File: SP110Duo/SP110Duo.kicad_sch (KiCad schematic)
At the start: 247 parts, among them SW1 RotaryEncoder_Switch, SW10 Switch w/LED, SW100 Switch w/LED, SW101 Switch w/LED, SW102 Switch w/LED, SW103 Switch w/LED, SW104 Switch w/LED, SW105 Switch w/LED, SW106 Switch w/LED, SW107 Switch w/LED, SW108 Switch w/LED, SW109 Switch w/LED, SW11 Switch w/LED, SW110 Switch w/LED, SW12 Switch w/LED, SW13 Switch w/LED, SW14 Switch w/LED, SW15 Switch w/LED, SW16 Switch w/LED, SW17 Switch w/LED, SW18 Switch w/LED, SW19 Switch w/LED, SW2 Switch w/LED, SW20 Switch w/LED, SW21 Switch w/LED, SW22 Switch w/LED, SW23 Switch w/LED, SW24 Switch w/LED, SW25 Switch w/LED, SW26 Switch w/LED, SW27 Switch w/LED, SW28 Switch w/LED, SW29 Switch w/LED, SW3 Switch w/LED, SW30 Switch w/LED, SW31 Switch w/LED, SW32 Switch w/LED, SW33 Switch w/LED, SW34 Switch w/LED, SW35 Switch w/LED, SW36 Switch w/LED, SW37 Switch w/LED, SW38 Switch w/LED, SW39 Switch w/LED, SW4 Switch w/LED, SW40 Switch w/LED, SW41 Switch w/LED, SW42 Switch w/LED, SW43 Switch w/LED, SW44 Switch w/LED, SW45 Switch w/LED, SW46 Switch w/LED, SW47 Switch w/LED, SW48 Switch w/LED, SW49 Switch w/LED, SW5 Switch w/LED, SW50 Switch w/LED, SW51 Switch w/LED, SW52 Switch w/LED, SW53 Switch w/LED, SW54 Switch w/LED, SW55 Switch w/LED, SW56 Switch w/LED, SW57 Switch w/LED, SW58 Switch w/LED, SW59 Switch w/LED, SW6 Switch w/LED, SW60 Switch w/LED, SW61 RotaryEncoder_Switch, SW62 Switch w/LED, SW63 Switch w/LED, SW64 Switch w/LED, SW65 Switch w/LED, SW66 Switch w/LED, SW67 Switch w/LED, SW68 Switch w/LED, SW69 Switch w/LED, SW7 Switch w/LED, SW70 Switch w/LED, SW71 Switch w/LED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

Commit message: Update
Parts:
- SW1: renamed from SW2; footprint Greenwood:Hotswap_MX_Plated_LED_1u -> KeebLib:Hotswap_MX_Plated_LED_1u
- SW10: renamed from SW11; footprint Greenwood:Hotswap_MX_Plated_LED_1u -> KeebLib:Hotswap_MX_Plated_LED_1u
- SW100: footprint Greenwood:Hotswap_MX_Plated_LED_1.25u -> KeebLib:Hotswap_MX_Plated_LED_1.25u
- SW101, SW80: footprint Greenwood:Hotswap_MX_Plated_LED_2.25u -> KeebLib:Hotswap_MX_Plated_LED_2.25u
- SW102, SW103, SW104, SW105, SW106, SW107, SW108, SW109, SW110, SW20, SW21, SW22, SW23, SW24, SW25, SW26, SW27, SW28, SW29, SW30, SW31, SW32, SW33, SW34, SW35, SW36, SW37, SW38, SW40, SW41, SW42, SW44, SW45, SW46, SW47, SW48, SW49, SW50, SW51, SW52, SW53, SW54, SW55, SW57, SW58, SW59, SW60, SW77, SW78, SW79, SW81, SW82, SW83, SW84, SW85, SW86, SW87, SW88, SW89, SW90, SW92, SW93, SW94, SW95, SW96: footprint Greenwood:Hotswap_MX_Plated_LED_1u -> KeebLib:Hotswap_MX_Plated_LED_1u
- SW11: renamed from SW12; footprint Greenwood:Hotswap_MX_Plated_LED_1u -> KeebLib:Hotswap_MX_Plated_LED_1u
- SW12: renamed from SW13; footprint Greenwood:Hotswap_MX_Plated_LED_1u -> KeebLib:Hotswap_MX_Plated_LED_1u
- SW13: renamed from SW14; footprint Greenwood:Hotswap_MX_Plated_LED_1u -> KeebLib:Hotswap_MX_Plated_LED_1u
- SW14: renamed from SW15; footprint Greenwood:Hotswap_MX_Plated_LED_1u -> KeebLib:Hotswap_MX_Plated_LED_1u
- SW15: renamed from SW16; footprint Greenwood:Hotswap_MX_Plated_LED_1u -> KeebLib:Hotswap_MX_Plated_LED_1u
- SW16: renamed from SW17; footprint Greenwood:Hotswap_MX_Plated_LED_1u -> KeebLib:Hotswap_MX_Plated_LED_1u
- SW17: renamed from SW18; footprint Greenwood:Hotswap_MX_Plated_LED_1u -> KeebLib:Hotswap_MX_Plated_LED_1u
- SW18: renamed from SW19; footprint Greenwood:Hotswap_MX_Plated_LED_1u -> KeebLib:Hotswap_MX_Plated_LED_1u
- SW19: renamed from SW1; footprint Greenwood:RotaryEncoder_Alps_EC11E-Switch_Vertical_H20mm_Centred -> KeebLib:RotaryEncoder_Alps_EC11E-Switch_Vertical_H20mm_Centred
- SW2: renamed from SW3; footprint Greenwood:Hotswap_MX_Plated_LED_1u -> KeebLib:Hotswap_MX_Plated_LED_1u
- SW3: renamed from SW4; footprint Greenwood:Hotswap_MX_Plated_LED_1u -> KeebLib:Hotswap_MX_Plated_LED_1u
- SW39, SW76: footprint Greenwood:Hotswap_MX_Plated_LED_2u_90deg -> KeebLib:Hotswap_MX_Plated_LED_2u_90deg
- SW4: renamed from SW5; footprint Greenwood:Hotswap_MX_Plated_LED_1u -> KeebLib:Hotswap_MX_Plated_LED_1u
- SW43, SW56, SW97, SW98: footprint Greenwood:Hotswap_MX_Plated_LED_1.5u -> KeebLib:Hotswap_MX_Plated_LED_1.5u
- SW5: renamed from SW6; footprint Greenwood:Hotswap_MX_Plated_LED_1u -> KeebLib:Hotswap_MX_Plated_LED_1u
- SW6: renamed from SW7; footprint Greenwood:Hotswap_MX_Plated_LED_1u -> KeebLib:Hotswap_MX_Plated_LED_1u
- SW61: renamed from SW62; footprint Greenwood:Hotswap_MX_Plated_LED_1.75u -> KeebLib:Hotswap_MX_Plated_LED_1.75u
- SW62: renamed from SW63; footprint Greenwood:Hotswap_MX_Plated_LED_1u -> KeebLib:Hotswap_MX_Plated_LED_1u
- SW63: renamed from SW64; footprint Greenwood:Hotswap_MX_Plated_LED_1u -> KeebLib:Hotswap_MX_Plated_LED_1u
- SW64: renamed from SW65; footprint Greenwood:Hotswap_MX_Plated_LED_1u -> KeebLib:Hotswap_MX_Plated_LED_1u
- SW65: renamed from SW66; footprint Greenwood:Hotswap_MX_Plated_LED_1u -> KeebLib:Hotswap_MX_Plated_LED_1u
- SW66: renamed from SW67; footprint Greenwood:Hotswap_MX_Plated_LED_1u -> KeebLib:Hotswap_MX_Plated_LED_1u
- SW67: renamed from SW68; footprint Greenwood:Hotswap_MX_Plated_LED_1u -> KeebLib:Hotswap_MX_Plated_LED_1u
- SW68: renamed from SW69; footprint Greenwood:Hotswap_MX_Plated_LED_1u -> KeebLib:Hotswap_MX_Plated_LED_1u
- SW69: renamed from SW70; footprint Greenwood:Hotswap_MX_Plated_LED_1u -> KeebLib:Hotswap_MX_Plated_LED_1u
- SW7: renamed from SW8; footprint Greenwood:Hotswap_MX_Plated_LED_1u -> KeebLib:Hotswap_MX_Plated_LED_1u
- SW70: renamed from SW71; footprint Greenwood:Hotswap_MX_Plated_LED_1u -> KeebLib:Hotswap_MX_Plated_LED_1u
- SW71: renamed from SW72; footprint Greenwood:Hotswap_MX_Plated_LED_1u -> KeebLib:Hotswap_MX_Plated_LED_1u
- SW72: renamed from SW73; footprint Greenwood:Hotswap_MX_Plated_LED_1u -> KeebLib:Hotswap_MX_Plated_LED_1u
- SW73: renamed from SW74; footprint Greenwood:Hotswap_MX_Plated_LED_2.25u -> KeebLib:Hotswap_MX_Plated_LED_2.25u
- SW74: renamed from SW75; footprint Greenwood:Hotswap_MX_Plated_LED_1u -> KeebLib:Hotswap_MX_Plated_LED_1u
- SW8: renamed from SW9; footprint Greenwood:Hotswap_MX_Plated_LED_1u -> KeebLib:Hotswap_MX_Plated_LED_1u
- SW9: renamed from SW10; footprint Greenwood:Hotswap_MX_Plated_LED_1u -> KeebLib:Hotswap_MX_Plated_LED_1u
- SW91: footprint Greenwood:Hotswap_MX_Plated_LED_1.75u -> KeebLib:Hotswap_MX_Plated_LED_1.75u
- SW99: footprint Greenwood:Hotswap_MX_Plated_LED_2.75u -> KeebLib:Hotswap_MX_Plated_LED_2.75u
- renumbered C5 to C10, C6 to C5, C7 to C6, C8 to C7, C9 to C8, C10 to C9, D2 to D1, D11 to D10, D12 to D11, D13 to D12, D14 to D13, D15 to D14, D16 to D15, D17 to D16, D18 to D17, D19 to D18, D1 to D19, D3 to D2, D4 to D3, D5 to D4, D6 to D5, D7 to D6, D62 to D61, D63 to D62, D64 to D63, D65 to D64, D66 to D65, D67 to D66, D68 to D67, D69 to D68, D70 to D69, D8 to D7, D71 to D70, D72 to D71, D73 to D72, D74 to D73, D75 to D74, D61 to D75, D9 to D8, D10 to D9, RESET to RESET1, SW61 to SW75, U3 to U2, U2 to U3

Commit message: change name
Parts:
- removed C5: 100uF, Capacitor_Tantalum_SMD:CP_EIA-6032-15_Kemet-U_Pad2.25x2.35mm_HandSolder, symbol Device:C_Polarized
- added R4, R5, R6: 5.1k, Resistor_SMD:R_1206_3216Metric_Pad1.30x1.75mm_HandSolder, symbol Device:R
- SW61: renamed from SW75; footprint Greenwood:EVQWGD001 -> KeebLib:RotaryEncoder_Alps_EC11E-Switch_Vertical_H20mm_Centred
- U3: footprint ScottoKeebs_MCU:Raspberry_Pi_Pico -> KeebLib:Raspberry_Pi_Pico_Flipped_No_Pads
- renumbered C10 to C5, D19 to D1, D9 to D10, D10 to D11, D11 to D12, D12 to D13, D13 to D14, D14 to D15, D15 to D16, D16 to D17, D17 to D18, D18 to D19, D1 to D2, D2 to D3, D3 to D4, D4 to D5, D5 to D6, D75 to D61, D61 to D62, D62 to D63, D63 to D64, D64 to D65, D65 to D66, D66 to D67, D67 to D68, D68 to D69, D6 to D7, D69 to D70, D70 to D71, D71 to D72, D72 to D73, D73 to D74, D74 to D75, D7 to D8, D8 to D9, H2 to H1, H3 to H2, H4 to H3, H5 to H4, H1 to H5, SW19 to SW1, SW9 to SW10, SW10 to SW11, SW11 to SW12, SW12 to SW13, SW13 to SW14, SW14 to SW15, SW15 to SW16, SW16 to SW17, SW17 to SW18, SW18 to SW19, SW1 to SW2, SW2 to SW3, SW3 to SW4, SW4 to SW5, SW5 to SW6, SW61 to SW62, SW62 to SW63, SW63 to SW64, SW64 to SW65, SW65 to SW66, SW66 to SW67, SW67 to SW68, SW68 to SW69, SW6 to SW7, SW69 to SW70, SW70 to SW71, SW71 to SW72, SW72 to SW73, SW73 to SW74, SW74 to SW75, SW7 to SW8, SW8 to SW9
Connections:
- net ENC1_A: now also C3.2, R4.1; no longer C3.1, SW1.A
- net ENC2_A: now also C5.2, U3.21 (GPIO16), R6.1; no longer C4.1, SW61.A, U3.19 (GPIO14)
- net ENC_B: now also C4.1, R5.1; no longer C5.1, SW1.B, SW61.B
- net GND: now also C3.1, C5.1; no longer C3.2, C5.2
- net OLED_CS: now also U3.22 (GPIO17); no longer U3.21 (GPIO16)
- net OLED_DC: now also U3.24 (GPIO18); no longer U3.22 (GPIO17)
- net OLED_RESET: now also U3.19 (GPIO14); no longer U3.24 (GPIO18)
- new net ROT1_A: R4.2, SW1.A
- new net ROT2_A: R6.2, SW61.A
- new net ROT_B: R5.2, SW1.B, SW61.B
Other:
- note added: "Encoders"
- note removed: "Encoder Filters"
- moved on the sheet: C3, C4, C5, C6, C7, C8, C9, D1, D61, H1, H2, H3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

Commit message: Update diode directions
Correct diode direction so that columns are not reversed in software.
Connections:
- net ROW0: now also D1.2 (A), D10.2 (A), D11.1 (K), D12.2 (A), D13.1 (K), D14.2 (A), D15.1 (K), D16.2 (A), D17.1 (K), D18.2 (A), D19.1 (K), D2.1 (K), D3.2 (A), D4.1 (K), D5.1 (K), D6.2 (A), D7.1 (K), D8.2 (A), D9.1 (K); no longer D1.1 (K), D10.1 (K), D11.2 (A), D12.1 (K), D13.2 (A), D14.1 (K), D15.2 (A), D16.1 (K), D17.2 (A), D18.1 (K), D19.2 (A), D2.2 (A), D3.1 (K), D4.2 (A), D5.2 (A), D6.1 (K), D7.2 (A), D8.1 (K), D9.2 (A)
- net ROW1: now also D20.2 (A), D21.1 (K), D22.2 (A), D23.1 (K), D24.1 (K), D25.2 (A), D26.1 (K), D27.2 (A), D28.1 (K), D29.2 (A), D30.1 (K), D31.2 (A), D32.1 (K), D33.2 (A), D34.1 (K), D35.2 (A), D36.1 (K), D37.2 (A), D38.1 (K); no longer D20.1 (K), D21.2 (A), D22.1 (K), D23.2 (A), D24.2 (A), D25.1 (K), D26.2 (A), D27.1 (K), D28.2 (A), D29.1 (K), D30.2 (A), D31.1 (K), D32.2 (A), D33.1 (K), D34.2 (A), D35.1 (K), D36.2 (A), D37.1 (K), D38.2 (A)
- net ROW2: now also D39.2 (A), D40.1 (K), D41.2 (A), D42.1 (K), D43.1 (K), D44.2 (A), D45.1 (K), D46.2 (A), D47.1 (K), D48.2 (A), D49.1 (K), D50.2 (A), D51.1 (K), D52.2 (A), D53.1 (K), D54.2 (A), D55.1 (K), D56.2 (A), D57.1 (K); no longer D39.1 (K), D40.2 (A), D41.1 (K), D42.2 (A), D43.2 (A), D44.1 (K), D45.2 (A), D46.1 (K), D47.2 (A), D48.1 (K), D49.2 (A), D50.1 (K), D51.2 (A), D52.1 (K), D53.2 (A), D54.1 (K), D55.2 (A), D56.1 (K), D57.2 (A)
- net ROW3: now also D58.1 (K), D59.2 (A), D60.1 (K), D61.2 (A), D62.1 (K), D63.2 (A), D64.1 (K), D65.2 (A), D66.1 (K), D67.2 (A), D68.1 (K), D69.2 (A), D70.1 (K), D71.2 (A), D72.1 (K), D73.2 (A), D74.1 (K), D75.1 (K); no longer D58.2 (A), D59.1 (K), D60.2 (A), D61.1 (K), D62.2 (A), D63.1 (K), D64.2 (A), D65.1 (K), D66.2 (A), D67.1 (K), D68.2 (A), D69.1 (K), D70.2 (A), D71.1 (K), D72.2 (A), D73.1 (K), D74.2 (A), D75.2 (A)
- net ROW4: now also D76.2 (A), D77.1 (K), D78.2 (A), D79.1 (K), D80.1 (K), D81.1 (K), D82.2 (A), D83.1 (K), D84.2 (A), D85.1 (K), D86.2 (A), D87.1 (K), D88.2 (A), D89.1 (K), D90.2 (A), D91.1 (K), D92.1 (K), D93.2 (A), D94.2 (A); no longer D76.1 (K), D77.2 (A), D78.1 (K), D79.2 (A), D80.2 (A), D81.2 (A), D82.1 (K), D83.2 (A), D84.1 (K), D85.2 (A), D86.1 (K), D87.2 (A), D88.1 (K), D89.2 (A), D90.1 (K), D91.2 (A), D92.2 (A), D93.1 (K), D94.1 (K)
- net ROW5: now also D100.1 (K), D101.1 (K), D102.2 (A), D103.1 (K), D104.2 (A), D105.1 (K), D106.2 (A), D107.1 (K), D108.1 (K), D109.2 (A), D110.1 (K), D95.1 (K), D96.2 (A), D97.2 (A), D98.1 (K), D99.1 (K); no longer D100.2 (A), D101.2 (A), D102.1 (K), D103.2 (A), D104.1 (K), D105.2 (A), D106.1 (K), D107.2 (A), D108.2 (A), D109.1 (K), D110.2 (A), D95.2 (A), D96.1 (K), D97.1 (K), D98.2 (A), D99.2 (A)
- net at SW92.2: now also D92.2 (A); no longer D92.1 (K)
- net at SW32.2: now also D32.2 (A); no longer D32.1 (K)
- net at SW61.S1: now also D61.1 (K); no longer D61.2 (A)
- net at SW108.2: now also D108.2 (A); no longer D108.1 (K)
- net at SW13.2: now also D13.2 (A); no longer D13.1 (K)
- net at SW22.2: now also D22.1 (K); no longer D22.2 (A)
- net at SW80.2: now also D80.2 (A); no longer D80.1 (K)
- net at SW17.2: now also D17.2 (A); no longer D17.1 (K)
- net at SW101.2: now also D101.2 (A); no longer D101.1 (K)
- net at SW75.2: now also D75.2 (A); no longer D75.1 (K)
- net at SW46.2: now also D46.1 (K); no longer D46.2 (A)
- net at SW82.2: now also D82.1 (K); no longer D82.2 (A)
- net at SW67.2: now also D67.1 (K); no longer D67.2 (A)
- net at SW76.2: now also D76.1 (K); no longer D76.2 (A)
- net at SW40.2: now also D40.2 (A); no longer D40.1 (K)
- net at SW14.2: now also D14.1 (K); no longer D14.2 (A)
- net at SW2.2: now also D2.2 (A); no longer D2.1 (K)
- net at SW66.2: now also D66.2 (A); no longer D66.1 (K)
- net at SW41.2: now also D41.1 (K); no longer D41.2 (A)
- net at SW79.2: now also D79.2 (A); no longer D79.1 (K)
- net at SW93.2: now also D93.1 (K); no longer D93.2 (A)
- net at SW45.2: now also D45.2 (A); no longer D45.1 (K)
- net at SW11.2: now also D11.2 (A); no longer D11.1 (K)
- net at SW99.2: now also D99.2 (A); no longer D99.1 (K)
- net at SW71.2: now also D71.1 (K); no longer D71.2 (A)
- net at SW96.2: now also D96.1 (K); no longer D96.2 (A)
- net at SW65.2: now also D65.1 (K); no longer D65.2 (A)
- net at SW57.2: now also D57.2 (A); no longer D57.1 (K)
- net at SW25.2: now also D25.1 (K); no longer D25.2 (A)
- net at SW77.2: now also D77.2 (A); no longer D77.1 (K)
- net at SW4.2: now also D4.2 (A); no longer D4.1 (K)
- net at SW60.2: now also D60.2 (A); no longer D60.1 (K)
- net at SW36.2: now also D36.2 (A); no longer D36.1 (K)
- net at SW81.2: now also D81.2 (A); no longer D81.1 (K)
- net at SW70.2: now also D70.2 (A); no longer D70.1 (K)
- net at SW87.2: now also D87.2 (A); no longer D87.1 (K)
- net at SW95.2: now also D95.2 (A); no longer D95.1 (K)
- net at SW48.2: now also D48.1 (K); no longer D48.2 (A)
- net at SW83.2: now also D83.2 (A); no longer D83.1 (K)
- net at SW52.2: now also D52.1 (K); no longer D52.2 (A)
- net at SW68.2: now also D68.2 (A); no longer D68.1 (K)
- net at SW107.2: now also D107.2 (A); no longer D107.1 (K)
- net at SW56.2: now also D56.1 (K); no longer D56.2 (A)
- net at SW39.2: now also D39.1 (K); no longer D39.2 (A)
- net at SW21.2: now also D21.2 (A); no longer D21.1 (K)
- net at SW94.2: now also D94.1 (K); no longer D94.2 (A)
- net at SW74.2: now also D74.2 (A); no longer D74.1 (K)
- net at SW72.2: now also D72.2 (A); no longer D72.1 (K)
- net at SW44.2: now also D44.1 (K); no longer D44.2 (A)
- net at SW35.2: now also D35.1 (K); no longer D35.2 (A)
- net at SW6.2: now also D6.1 (K); no longer D6.2 (A)
- net at SW15.2: now also D15.2 (A); no longer D15.1 (K)
- net at SW3.2: now also D3.1 (K); no longer D3.2 (A)
- net at SW110.2: now also D110.2 (A); no longer D110.1 (K)
- net at SW33.2: now also D33.1 (K); no longer D33.2 (A)
- net at SW59.2: now also D59.1 (K); no longer D59.2 (A)
- net at SW55.2: now also D55.2 (A); no longer D55.1 (K)
- net at SW98.2: now also D98.2 (A); no longer D98.1 (K)
- net at SW88.2: now also D88.1 (K); no longer D88.2 (A)
- net at SW91.2: now also D91.2 (A); no longer D91.1 (K)
- net at SW78.2: now also D78.1 (K); no longer D78.2 (A)
- net at SW20.2: now also D20.1 (K); no longer D20.2 (A)
- net at SW42.2: now also D42.2 (A); no longer D42.1 (K)
- net at SW7.2: now also D7.2 (A); no longer D7.1 (K)
- net at SW105.2: now also D105.2 (A); no longer D105.1 (K)
- net at SW43.2: now also D43.2 (A); no longer D43.1 (K)
- net at SW53.2: now also D53.2 (A); no longer D53.1 (K)
- net at SW9.2: now also D9.2 (A); no longer D9.1 (K)
- net at SW37.2: now also D37.1 (K); no longer D37.2 (A)
- net at SW28.2: now also D28.2 (A); no longer D28.1 (K)
- net at SW62.2: now also D62.2 (A); no longer D62.1 (K)
- net at SW84.2: now also D84.1 (K); no longer D84.2 (A)
- net at SW8.2: now also D8.1 (K); no longer D8.2 (A)
- net at SW26.2: now also D26.2 (A); no longer D26.1 (K)
- net at SW18.2: now also D18.1 (K); no longer D18.2 (A)
- net at SW97.2: now also D97.1 (K); no longer D97.2 (A)
- net at SW23.2: now also D23.2 (A); no longer D23.1 (K)
- net at SW69.2: now also D69.1 (K); no longer D69.2 (A)
- net at SW19.2: now also D19.2 (A); no longer D19.1 (K)
- net at SW102.2: now also D102.1 (K); no longer D102.2 (A)
- net at SW49.2: now also D49.2 (A); no longer D49.1 (K)
- net at SW12.2: now also D12.1 (K); no longer D12.2 (A)
- net at SW85.2: now also D85.2 (A); no longer D85.1 (K)
- net at SW51.2: now also D51.2 (A); no longer D51.1 (K)
- net at SW103.2: now also D103.2 (A); no longer D103.1 (K)
- net at SW86.2: now also D86.1 (K); no longer D86.2 (A)
- net at SW38.2: now also D38.2 (A); no longer D38.1 (K)
- net at SW63.2: now also D63.1 (K); no longer D63.2 (A)
- net at SW30.2: now also D30.2 (A); no longer D30.1 (K)
- net at SW106.2: now also D106.1 (K); no longer D106.2 (A)
- net at SW50.2: now also D50.1 (K); no longer D50.2 (A)
- net at SW104.2: now also D104.1 (K); no longer D104.2 (A)
- net at SW90.2: now also D90.1 (K); no longer D90.2 (A)
- net at SW5.2: now also D5.2 (A); no longer D5.1 (K)
- net at SW109.2: now also D109.1 (K); no longer D109.2 (A)
- net at SW34.2: now also D34.2 (A); no longer D34.1 (K)
- net at SW100.2: now also D100.2 (A); no longer D100.1 (K)
- net at SW89.2: now also D89.2 (A); no longer D89.1 (K)
- net at SW16.2: now also D16.1 (K); no longer D16.2 (A)
- net at SW29.2: now also D29.1 (K); no longer D29.2 (A)
- net at SW1.S1: now also D1.1 (K); no longer D1.2 (A)
- net at SW64.2: now also D64.2 (A); no longer D64.1 (K)
- net at SW58.2: now also D58.2 (A); no longer D58.1 (K)
- net at SW24.2: now also D24.2 (A); no longer D24.1 (K)
- net at SW47.2: now also D47.2 (A); no longer D47.1 (K)
- net at SW27.2: now also D27.1 (K); no longer D27.2 (A)
- net at SW73.2: now also D73.1 (K); no longer D73.2 (A)
- net at SW31.2: now also D31.1 (K); no longer D31.2 (A)
- net at SW10.2: now also D10.1 (K); no longer D10.2 (A)
- net at SW54.2: now also D54.1 (K); no longer D54.2 (A)
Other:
- moved on the sheet: D1, D10, D100, D101, D102, D103, D104, D105, D106, D107, D108, D109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

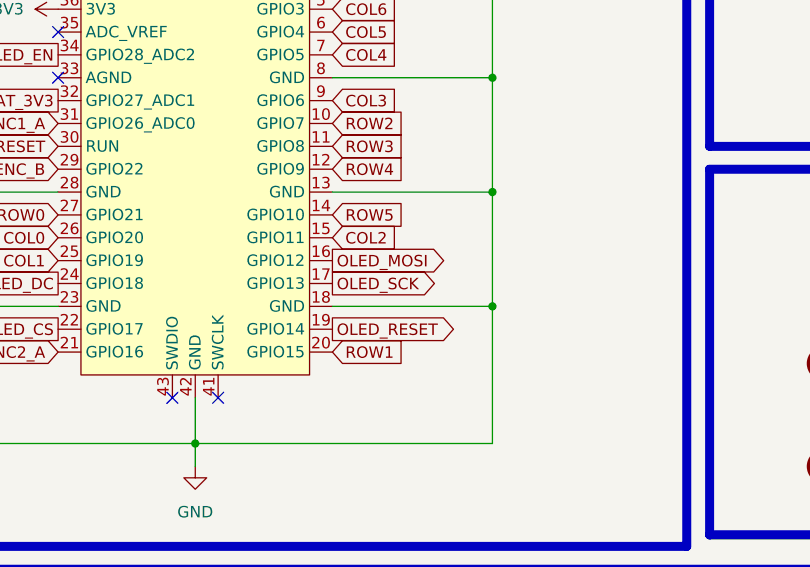
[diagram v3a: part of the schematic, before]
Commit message: Fix crossed pins for display
Update so that SPI pins are in correct place
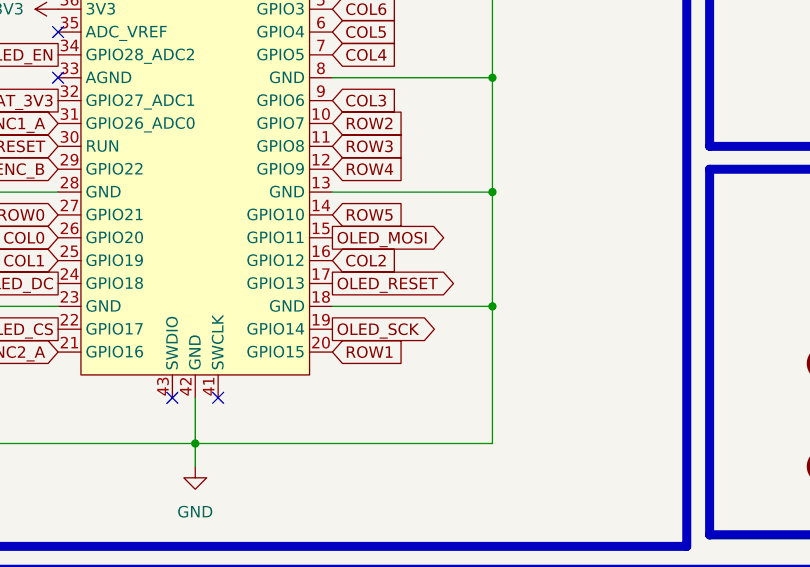
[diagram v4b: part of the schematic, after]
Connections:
- net COL2: now also U3.16 (GPIO12); no longer U3.15 (GPIO11)
- net OLED_MOSI: now also U3.15 (GPIO11); no longer U3.16 (GPIO12)
- net OLED_RESET: now also U3.17 (GPIO13); no longer U3.19 (GPIO14)
- net OLED_SCK: now also U3.19 (GPIO14); no longer U3.17 (GPIO13)
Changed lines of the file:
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@@
     )
   )
-  (global_label "COL2" (shape input) (at 175.26 151.13 0) (fields_autoplaced)
-    (effects (font (size 1.27 1.27)) (justify left))
-    (property "Intersheetrefs" "${INTERSHEET_REFS}" (at 183.0833 151.13 0)
+  (global_label "COL2" (shape input) (at 175.26 153.67 0) (fields_autoplaced)
+    (effects (font (size 1.27 1.27)) (justify left))
+    (property "Intersheetrefs" "${INTERSHEET_REFS}" (at 183.0833 153.67 0)
       (effects (font (size 1.27 1.27)) (justify left) hide)
     )
@@
     )
   )
-  (global_label "OLED_SCK" (shape output) (at 175.26 156.21 0) (fields_autoplaced)
-    (effects (font (size 1.27 1.27)) (justify left))
-    (property "Intersheetrefs" "${INTERSHEET_REFS}" (at 187.7399 156.21 0)
-      (effects (font (size 1.27 1.27)) (justify left) hide)
-    )
-  )
   (global_label "COL1" (shape input) (at 144.78 153.67 180) (fields_autoplaced)
     (effects (font (size 1.27 1.27)) (justify right))
@@
     )
   )
+  (global_label "OLED_SCK" (shape output) (at 175.26 161.29 0) (fields_autoplaced)
+    (effects (font (size 1.27 1.27)) (justify left))
+    (property "Intersheetrefs" "${INTERSHEET_REFS}" (at 187.7399 161.29 0)
+      (effects (font (size 1.27 1.27)) (justify left) hide)
+    )
+  )
   (global_label "COL3" (shape input) (at 175.26 135.89 0) (fields_autoplaced)
     (effects (font (size 1.27 1.27)) (justify left))
@@
     )
   )
-  (global_label "OLED_MOSI" (shape output) (at 175.26 153.67 0) (fields_autoplaced)
-    (effects (font (size 1.27 1.27)) (justify left))
-    (property "Intersheetrefs" "${INTERSHEET_REFS}" (at 188.5866 153.67 0)
+  (global_label "OLED_MOSI" (shape output) (at 175.26 151.13 0) (fields_autoplaced)
+    (effects (font (size 1.27 1.27)) (justify left))
+    (property "Intersheetrefs" "${INTERSHEET_REFS}" (at 188.5866 151.13 0)
+      (effects (font (size 1.27 1.27)) (justify left) hide)
+    )
+  )
+  (global_label "OLED_RESET" (shape output) (at 175.26 156.21 0) (fields_autoplaced)
+    (effects (font (size 1.27 1.27)) (justify left))
+    (property "Intersheetrefs" "${INTERSHEET_REFS}" (at 189.7355 156.21 0)
       (effects (font (size 1.27 1.27)) (justify left) hide)
     )
@@
     )
   )
-  (global_label "OLED_RESET" (shape output) (at 175.26 161.29 0) (fields_autoplaced)
-    (effects (font (size 1.27 1.27)) (justify left))
-    (property "Intersheetrefs" "${INTERSHEET_REFS}" (at 189.7355 161.29 0)
-      (effects (font (size 1.27 1.27)) (justify left) hide)
-    )
-  )
